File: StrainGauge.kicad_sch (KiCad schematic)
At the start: 34 parts, among them J1 Conn_01x04, J2 502585-0470, U1 INA333xxDGK, U2 REF2025, U3 OPA310xDBV, U4 OPA310xDBV

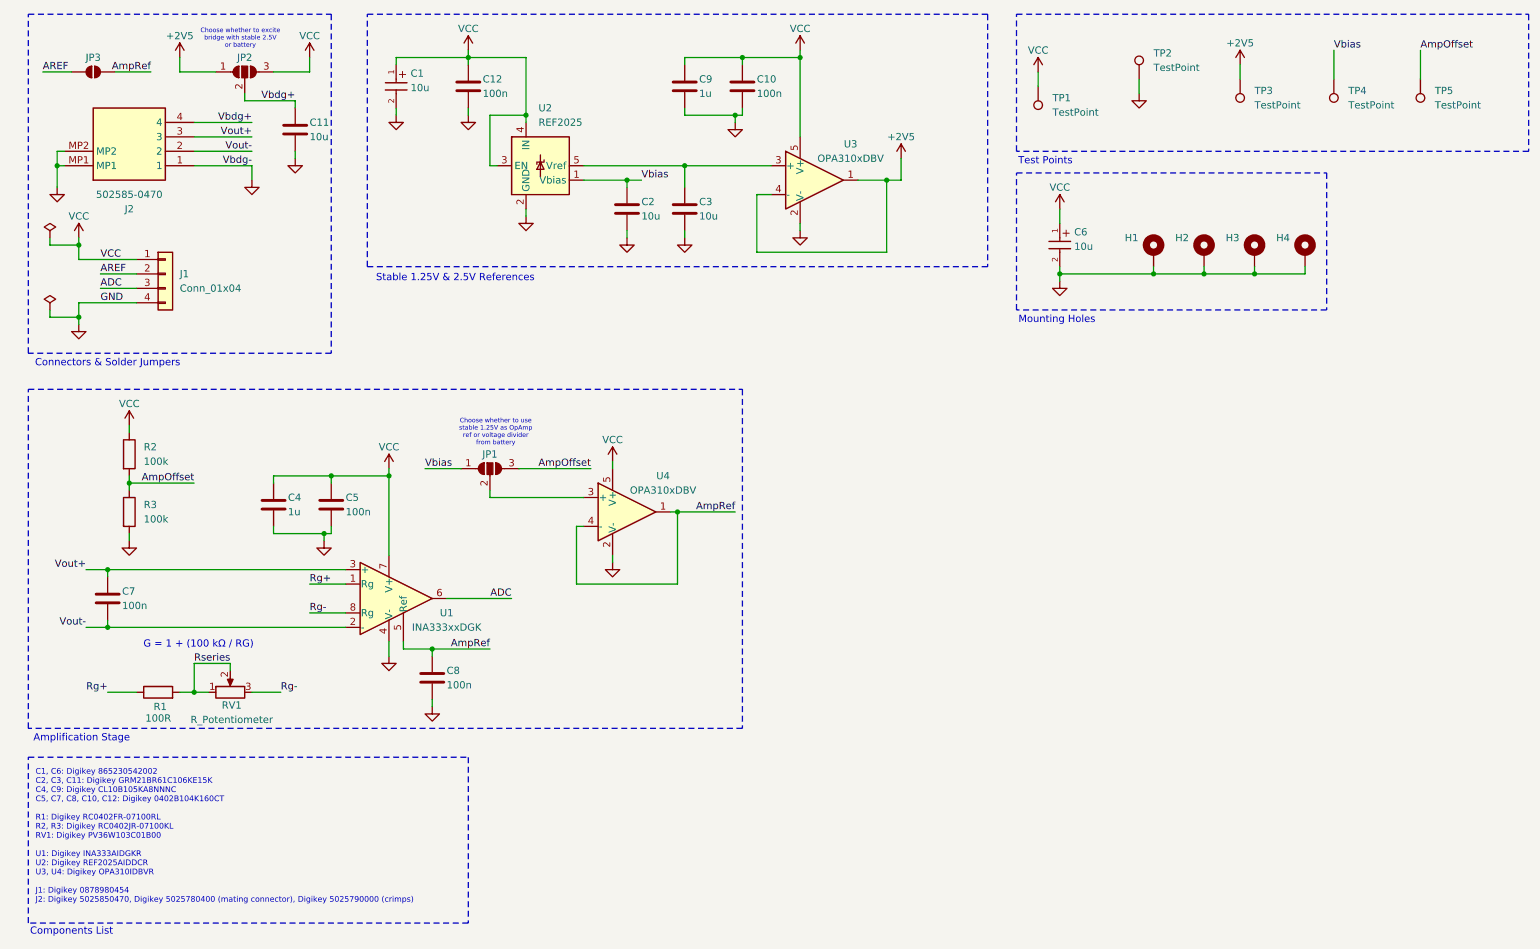
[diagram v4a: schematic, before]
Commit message: added power connector for external battery
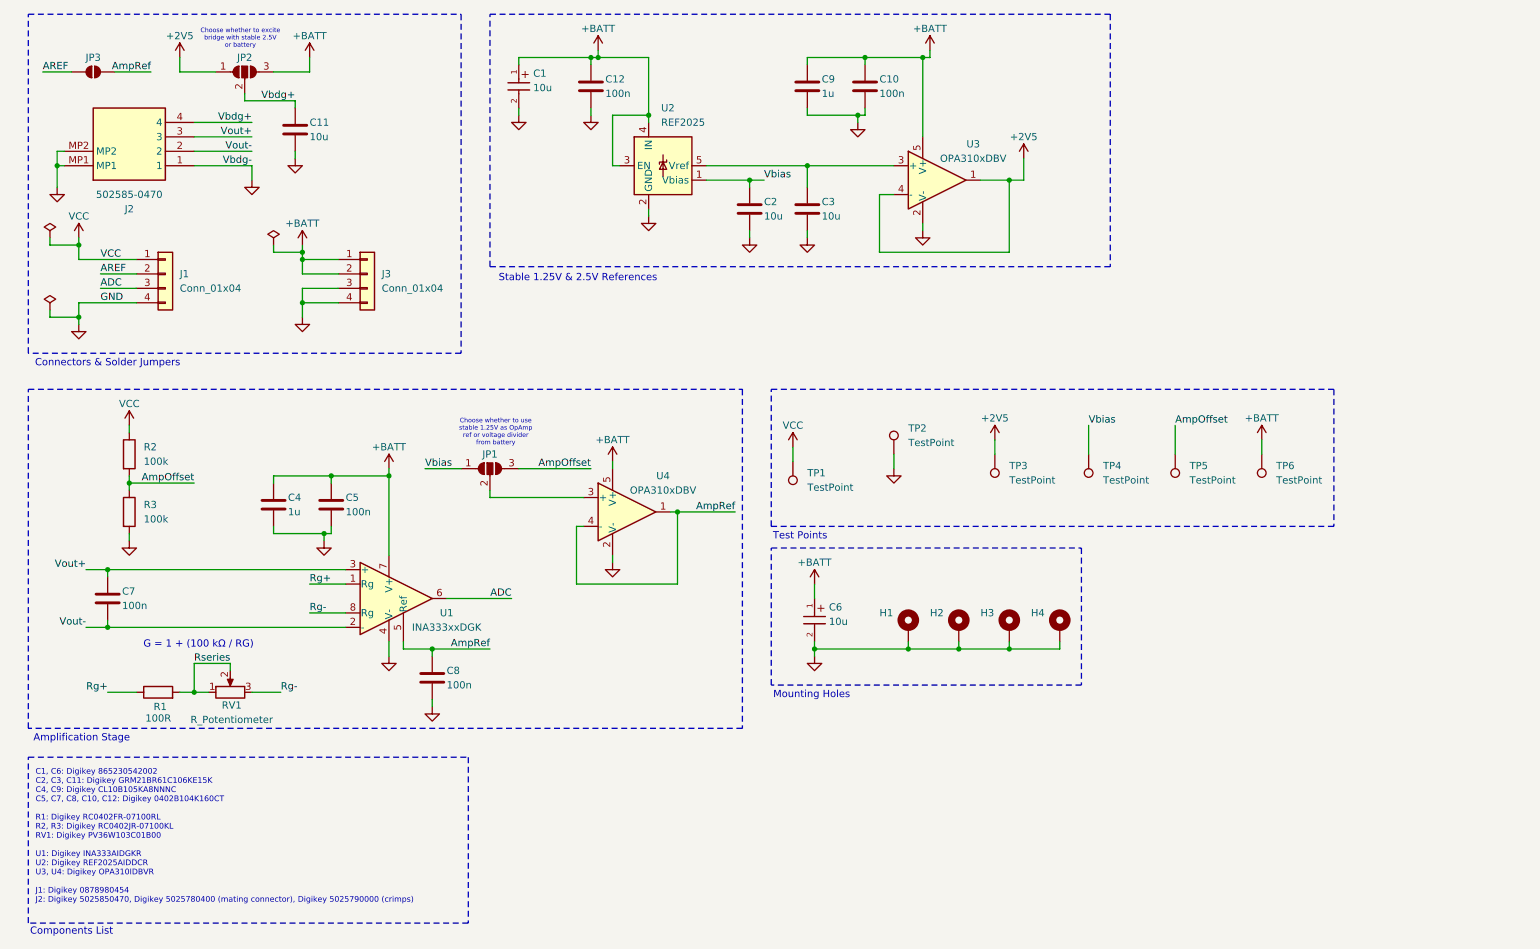
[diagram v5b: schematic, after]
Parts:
- added J3: Conn_01x04, Connector_PinSocket_2.54mm:PinSocket_1x04_P2.54mm_Vertical, symbol Connector_Generic:Conn_01x04
- added TP6: TestPoint, TestPoint:TestPoint_Pad_2.0x2.0mm, symbol Connector:TestPoint
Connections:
- net GND: now also J3.3 (Pin_3), J3.4 (Pin_4)
- net VCC: no longer C1.1, C10.1, C12.1, C4.1, C5.1, C6.1, C9.1, JP2.3 (B), U1.7 (V+), U2.3 (EN), U2.4 (IN), U3.5 (V+), U4.5 (V+)
- new net +BATT: C1.1, C10.1, C12.1, C4.1, C5.1, C6.1, C9.1, J3.1 (Pin_1), J3.2 (Pin_2), JP2.3 (B), TP6.1, U1.7 (V+), U2.3 (EN), U2.4 (IN), U3.5 (V+), U4.5 (V+)
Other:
- moved on the sheet: C1, C10, C12, C2, C3, C6, C9, H1, H2, H3, H4, TP1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

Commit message: added test note #1
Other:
- note added: "In the PCB manufactured at EPFL, one of the vias (connecting the VBATT pad to the rest of the circuit) probably broke, causing a bad connection which lead to the rest of the board not being powered. To fix this, an extra jumper was used to connect the VBATT test pad to the C1 positive pin. The voltage regulating part of the PCB works great."
- note added: "Testing Note #1:"
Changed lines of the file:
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@@
+	)
+	(rectangle
+		(start 209.55 29.21)
+		(end 260.35 53.34)
+		(stroke
+			(width 0)
+			(type dash_dot)
+		)
+		(fill
+			(type none)
+		)
 	)
 	(rectangle
@@
 		)
 	)
+	(text "Testing Note #1:\n"
+		(exclude_from_sim no)
+		(at 211.074 31.496 0)
+		(effects
+			(font
+				(size 1.27 1.27)
+				(thickness 0.254)
+				(bold yes)
+				(color 194 0 0 1)
+			)
+			(justify left)
+		)
+	)
 	(text "C1, C6: Digikey 865230542002\nC2, C3, C11: Digikey GRM21BR61C106KE15K\nC4, C9: Digikey CL10B105KA8NNNC\nC5, C7, C8, C10, C12: Digikey 0402B104K160CT\n\nR1: Digikey RC0402FR-07100RL\nR2, R3: Digikey RC0402JR-07100KL\nRV1: Digikey PV36W103C01B00\n\nU1: Digikey INA333AIDGKR\nU2: Digikey REF2025AIDDCR\nU3, U4: Digikey OPA310IDBVR\n\nJ1: Digikey 0878980454\nJ2: Digikey 5025850470, Digikey 5025780400 (mating connector), Digikey 5025790000 (crimps)"
 		(exclude_from_sim no)
@@
 		)
 	)
+	(text "\n\nIn the PCB manufactured at EPFL, one of\nthe vias (connecting the VBATT pad to the rest\nof the circuit) probably broke, causing a bad\nconnection which lead to the rest of the board\nnot being powered. To fix this, an extra jumper\nwas used to connect the VBATT test pad to the\nC1 positive pin. The voltage regulating part of\nthe PCB works great."
+		(exclude_from_sim no)
+		(at 211.074 41.148 0)
+		(effects
+			(font
+				(size 1.27 1.27)
+				(color 194 0 0 1)
+			)
+			(justify left)
+		)
+	)

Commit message: added test note #2
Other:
- note added: "It turns out that more than 1 via was broken, and another trace was broken (seen on microscope), so many extra jumpers were added on the PCB. This probably wouldn't have happened in a higher quality PCB manufacturing facility, this could be added as a useful note for manufacturing constaints in the future."
- note added: "Testing Note #2:"
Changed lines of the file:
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@@
+	)
+	(rectangle
+		(start 209.55 55.88)
+		(end 260.35 76.2)
+		(stroke
+			(width 0)
+			(type dash_dot)
+		)
+		(fill
+			(type none)
+		)
 	)
 	(rectangle
@@
 		)
 	)
+	(text "\n\nIt turns out that more than 1 via was broken,\nand another trace was broken (seen on\nmicroscope), so many extra jumpers were\nadded on the PCB. This probably wouldn't have\nhappened in a higher quality PCB manufacturing\nfacility, this could be added as a useful note\nfor manufacturing constaints in the future."
+		(exclude_from_sim no)
+		(at 211.074 65.532 0)
+		(effects
+			(font
+				(size 1.27 1.27)
+				(color 194 0 0 1)
+			)
+			(justify left)
+		)
+	)
 	(text "Amplification Stage"
 		(exclude_from_sim no)
@@
 		)
 	)
+	(text "Testing Note #2:\n"
+		(exclude_from_sim no)
+		(at 211.074 58.166 0)
+		(effects
+			(font
+				(size 1.27 1.27)
+				(thickness 0.254)
+				(bold yes)
+				(color 194 0 0 1)
+			)
+			(justify left)
+		)
+	)

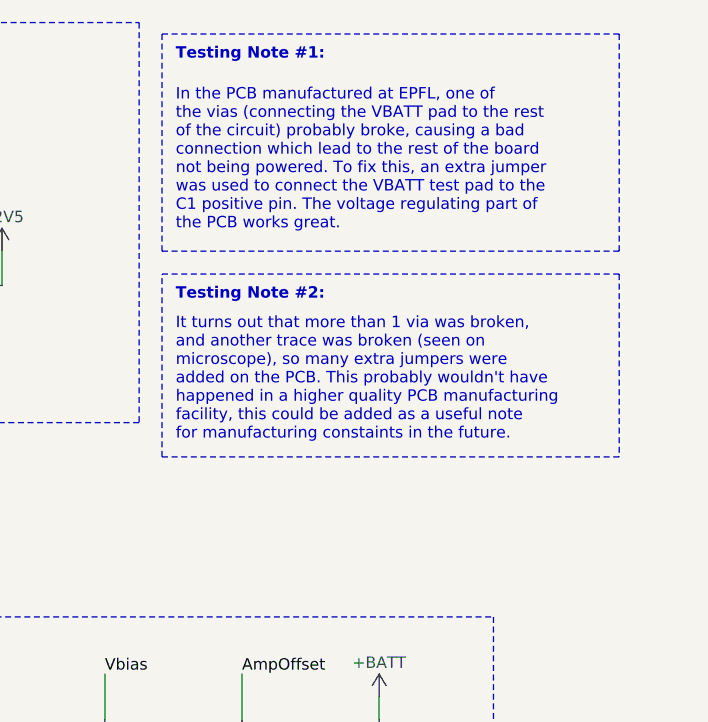
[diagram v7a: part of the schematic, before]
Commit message: added test note #3 + completed revision 1.0
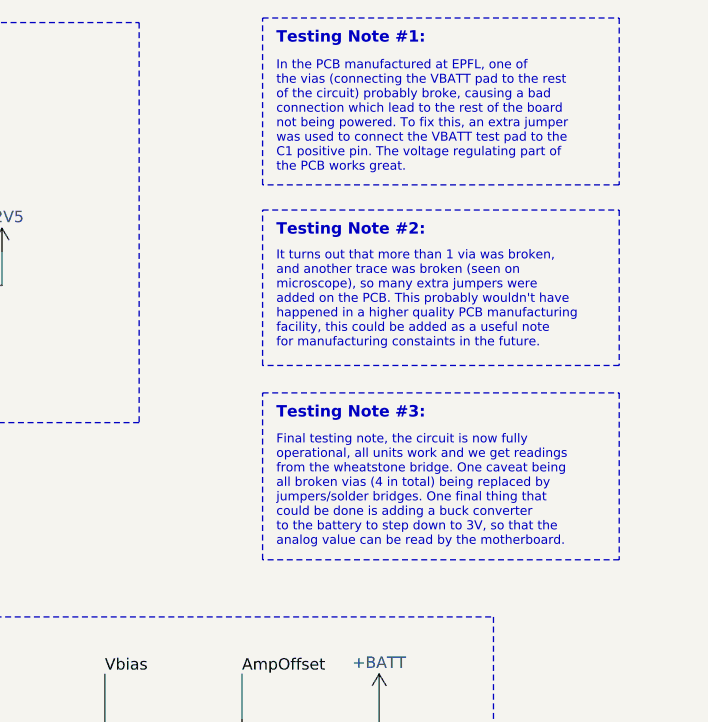
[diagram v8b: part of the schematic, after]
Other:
- note added: "Final testing note, the circuit is now fully operational, all units work and we get readings from the wheatstone bridge. One caveat being all broken vias (4 in total) being replaced by jumpers/solder bridges. One final thing that could be done is adding a buck converter to the battery to step down to 3V, so that the analog value can be read by the motherboard."
- note added: "Testing Note #3:"
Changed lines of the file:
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@@
 		(title "Strain Sensor")
 		(date "2025-03-11")
-		(rev "1")
+		(rev "1.0")
 		(company "EPFL")
-		(comment 4 "Added components list")
+		(comment 4 "Rev 1.0 complete.")
 	)
 	(junction
@@
 			(width 0)
 			(type default)
+		)
+	)
+	(rectangle
+		(start 220.726 69.088)
+		(end 260.35 87.63)
+		(stroke
+			(width 0)
+			(type dash_dot)
+		)
+		(fill
+			(type none)
 		)
 	)
@@
 	)
 	(rectangle
-		(start 209.55 29.21)
-		(end 260.35 53.34)
+		(start 220.726 27.432)
+		(end 260.35 45.974)
 		(stroke
 			(width 0)
@@
 	)
 	(rectangle
-		(start 209.55 55.88)
-		(end 260.35 76.2)
+		(start 220.726 48.768)
+		(end 260.35 66.04)
 		(stroke
 			(width 0)
@@
 		(fill
 			(type none)
+		)
+	)
+	(text "Final testing note, the circuit is now fully\noperational, all units work and we get readings\nfrom the wheatstone bridge. One caveat being\nall broken vias (4 in total) being replaced by\njumpers/solder bridges. One final thing that\ncould be done is adding a buck converter\nto the battery to step down to 3V, so that the\nanalog value can be read by the motherboard."
+		(exclude_from_sim no)
+		(at 222.25 80.01 0)
+		(effects
+			(font
+				(size 1 1)
+				(color 194 0 0 1)
+			)
+			(justify left)
 		)
 	)
@@
 	(text "Testing Note #1:\n"
 		(exclude_from_sim no)
-		(at 211.074 31.496 0)
+		(at 222.25 29.718 0)
 		(effects
 			(font
@@
 	(text "\n\nIn the PCB manufactured at EPFL, one of\nthe vias (connecting the VBATT pad to the rest\nof the circuit) probably broke, causing a bad\nconnection which lead to the rest of the board\nnot being powered. To fix this, an extra jumper\nwas used to connect the VBATT test pad to the\nC1 positive pin. The voltage regulating part of\nthe PCB works great."
 		(exclude_from_sim no)
-		(at 211.074 41.148 0)
+		(at 222.25 36.83 0)
 		(effects
 			(font
-				(size 1.27 1.27)
+				(size 1 1)
 				(color 194 0 0 1)
 			)
@@
 		)
 	)
-	(text "\n\nIt turns out that more than 1 via was broken,\nand another trace was broken (seen on\nmicroscope), so many extra jumpers were\nadded on the PCB. This probably wouldn't have\nhappened in a higher quality PCB manufacturing\nfacility, this could be added as a useful note\nfor manufacturing constaints in the future."
+	(text "Testing Note #3:\n"
 		(exclude_from_sim no)
-		(at 211.074 65.532 0)
+		(at 222.25 71.374 0)
 		(effects
 			(font
 				(size 1.27 1.27)
+				(thickness 0.254)
+				(bold yes)
+				(color 194 0 0 1)
+			)
+			(justify left)
+		)
+	)
+	(text "\n\nIt turns out that more than 1 via was broken,\nand another trace was broken (seen on\nmicroscope), so many extra jumpers were\nadded on the PCB. This probably wouldn't have\nhappened in a higher quality PCB manufacturing\nfacility, this could be added as a useful note\nfor manufacturing constaints in the future."
+		(exclude_from_sim no)
+		(at 222.25 57.15 0)
+		(effects
+			(font
+				(size 1 1)
 				(color 194 0 0 1)
 			)
@@
 	(text "Testing Note #2:\n"
 		(exclude_from_sim no)
-		(at 211.074 58.166 0)
+		(at 222.25 51.054 0)
 		(effects
 			(font
